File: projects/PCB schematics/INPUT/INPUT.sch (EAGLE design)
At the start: 84 parts, among them IC1 OP11D, IC10 74AHC1G32DCK, IC13 OP11D, IC14 74AHC1G32DCK, IC17 OP11D, IC18 74AHC1G32DCK, IC19 OP11D, IC20 OP11D, IC3 OP11D, IC4 OP11D, IC5 OP11D, IC6 74AHC1G32DCK, IC7 OP11D, IC8 OP11D, IC9 74AHC1G32DCK

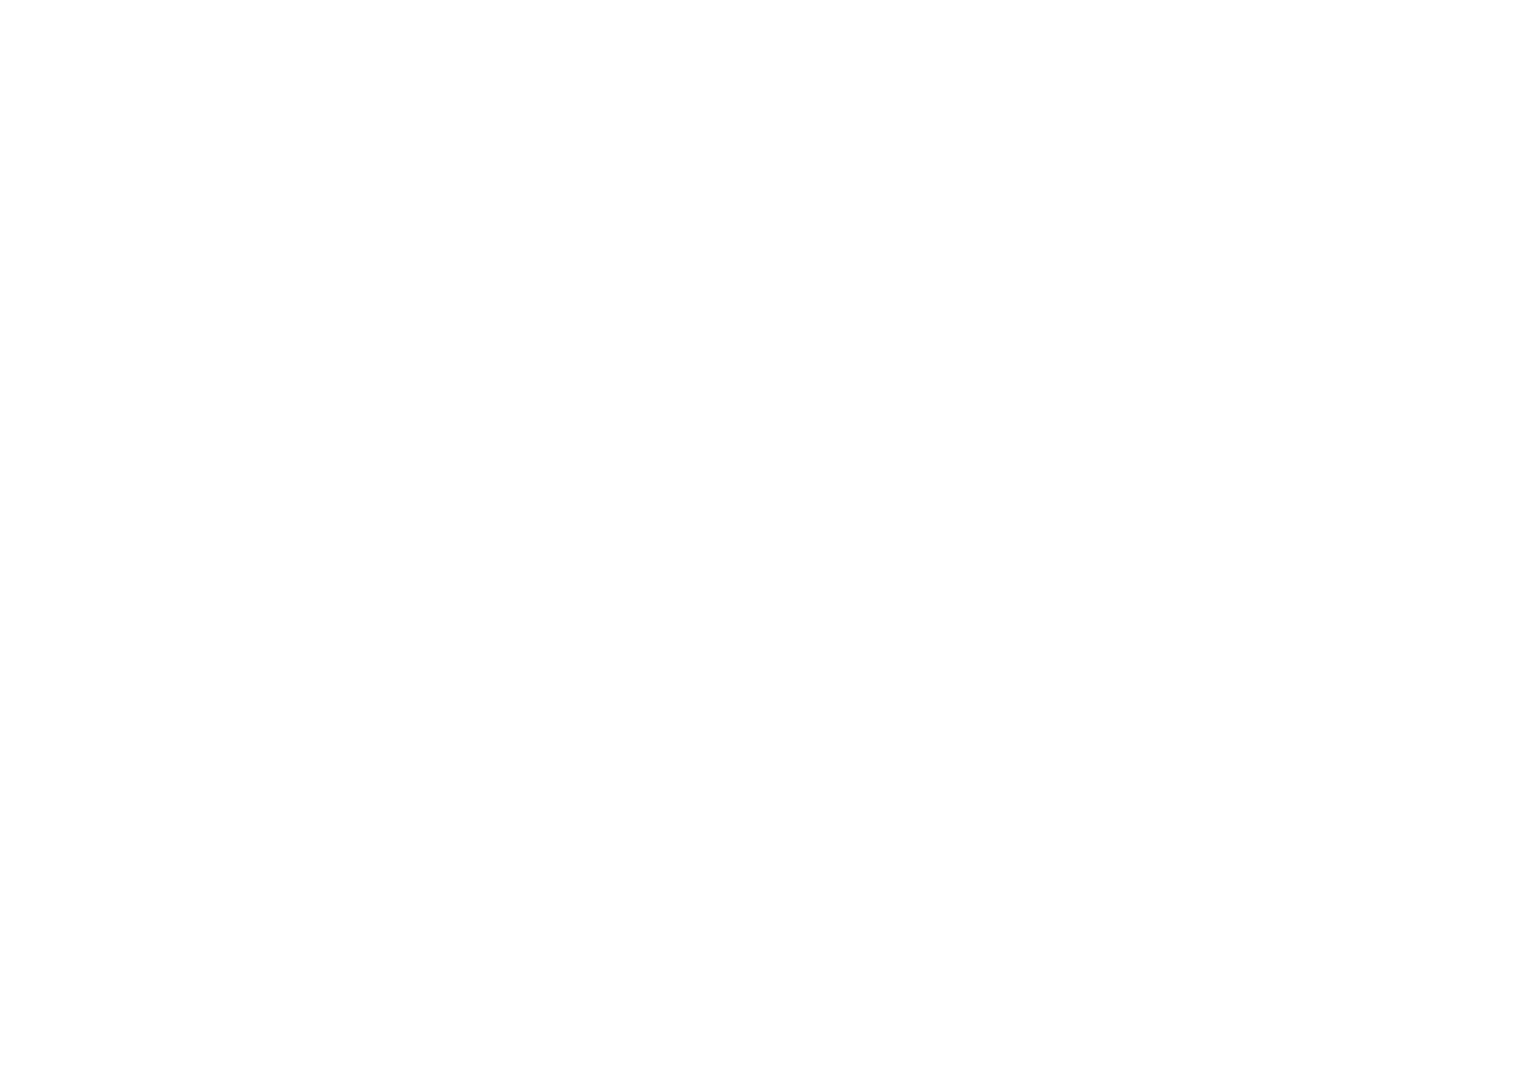
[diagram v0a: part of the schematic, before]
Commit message: BSPD - Schematic revision/component revision.
During ESF, schematics chosen used European part libraries.
These were updated to US symbols, with appropriate final parts sourced
to allow builds of both SOP8 and DIL-8 packages.
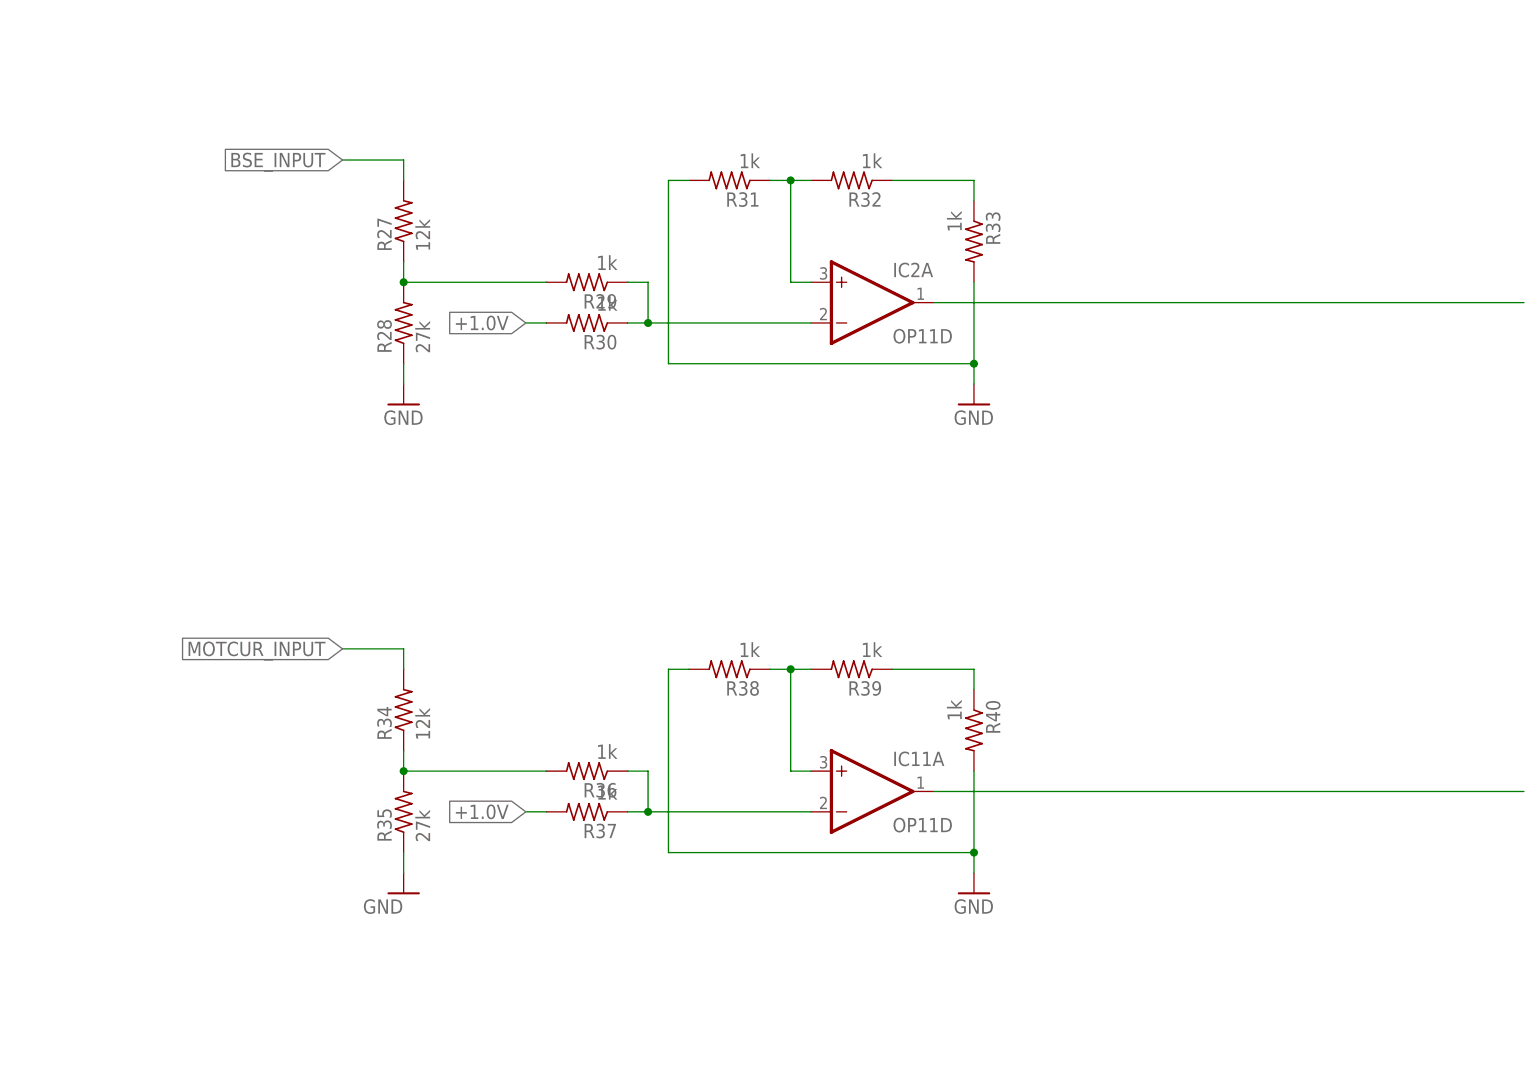
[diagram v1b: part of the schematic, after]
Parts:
- added IC11, IC2: OP11D, linear:OP11D
- added R27, R34: 12k, rcl:R-US_R0805
- added R28, R35: 27k, rcl:R-US_R0805
- added R29, R30, R31, R32, R33, R36, R37, R38, R39, R40: 1k, rcl:R-US_R0805
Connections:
- new net BSE_INPUT: R27.2
- new net BSE_PROCESSED: IC2A.OUT
- new net MOTCUR_INPUT: R34.2
- new net MOTCUR_PROCESSED: IC11A.OUT
- new net N$19: IC2A.+IN, R31.1, R32.2
- new net N$21: R27.1, R28.2, R29.2
- new net N$22: R32.1, R33.1
- new net N$25: IC2A.-IN, R29.1, R30.1
- new net N$32: IC11A.+IN, R38.1, R39.2
- new net N$33: R34.1, R35.2, R36.2
- new net N$36: R39.1, R40.1
- new net N$37: IC11A.-IN, R36.1, R37.1
- net +1.0V: now also R30.2, R37.2
- net GND: now also R28.1, R31.2, R33.2, R35.1, R38.2, R40.2
